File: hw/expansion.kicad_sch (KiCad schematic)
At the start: 2 parts

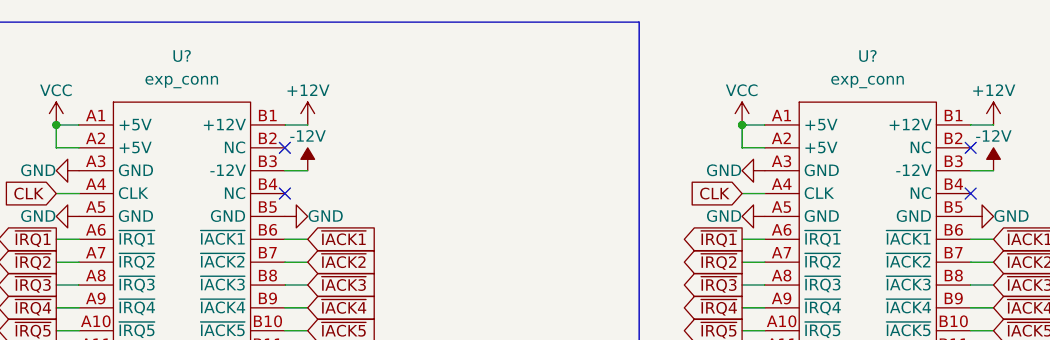
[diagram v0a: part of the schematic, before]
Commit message: fixed ERC errors
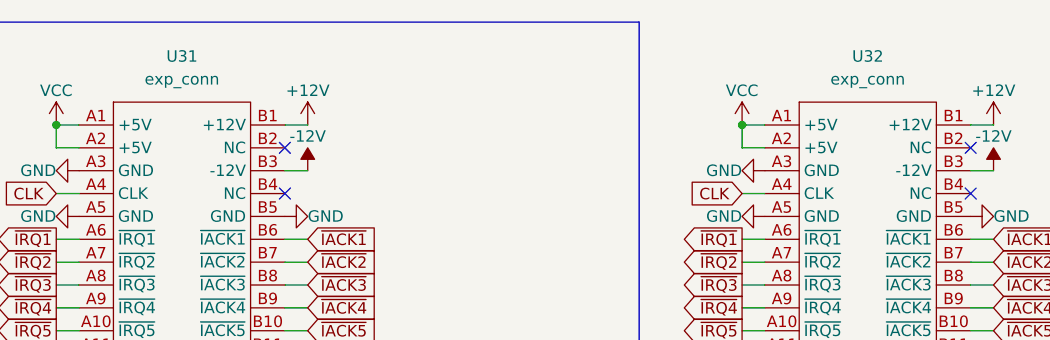
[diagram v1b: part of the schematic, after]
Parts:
- gave numbers to parts that had none: 2
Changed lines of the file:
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@@
   (symbol (lib_id "power:-12V") (at 124.46 33.02 0) (unit 1)
     (in_bom yes) (on_board yes)
-    (property "Reference" "#PWR?" (id 0) (at 124.46 30.48 0)
+    (property "Reference" "#PWR086" (id 0) (at 124.46 30.48 0)
       (effects (font (size 1.27 1.27)) hide)
     )
@@
   (symbol (lib_id "power:GND") (at 121.92 38.1 90) (unit 1)
     (in_bom yes) (on_board yes)
-    (property "Reference" "#PWR?" (id 0) (at 128.27 38.1 0)
+    (property "Reference" "#PWR084" (id 0) (at 128.27 38.1 0)
       (effects (font (size 1.27 1.27)) hide)
     )
@@
   (symbol (lib_id "power:VCC") (at 96.52 27.94 0) (unit 1)
     (in_bom yes) (on_board yes)
-    (property "Reference" "#PWR?" (id 0) (at 96.52 31.75 0)
+    (property "Reference" "#PWR081" (id 0) (at 96.52 31.75 0)
       (effects (font (size 1.27 1.27)) hide)
     )
@@
   (symbol (lib_id "m68kcomp2:exp_conn") (at 110.49 24.13 0) (unit 1)
     (in_bom yes) (on_board yes) (fields_autoplaced)
-    (property "Reference" "U?" (id 0) (at 110.49 20.32 0))
+    (property "Reference" "U31" (id 0) (at 110.49 20.32 0))
     (property "Value" "exp_conn" (id 1) (at 110.49 22.86 0))
     (property "Footprint" "" (id 2) (at 110.49 24.13 0)
@@
   (symbol (lib_id "power:VCC") (at 172.72 27.94 0) (unit 1)
     (in_bom yes) (on_board yes)
-    (property "Reference" "#PWR?" (id 0) (at 172.72 31.75 0)
+    (property "Reference" "#PWR087" (id 0) (at 172.72 31.75 0)
       (effects (font (size 1.27 1.27)) hide)
     )
@@
   (symbol (lib_id "power:+12V") (at 124.46 27.94 0) (unit 1)
     (in_bom yes) (on_board yes)
-    (property "Reference" "#PWR?" (id 0) (at 124.46 31.75 0)
+    (property "Reference" "#PWR085" (id 0) (at 124.46 31.75 0)
       (effects (font (size 1.27 1.27)) hide)
     )
@@
   (symbol (lib_id "power:GND") (at 99.06 38.1 270) (unit 1)
     (in_bom yes) (on_board yes)
-    (property "Reference" "#PWR?" (id 0) (at 92.71 38.1 0)
+    (property "Reference" "#PWR083" (id 0) (at 92.71 38.1 0)
       (effects (font (size 1.27 1.27)) hide)
     )
@@
   (symbol (lib_id "power:GND") (at 198.12 38.1 90) (unit 1)
     (in_bom yes) (on_board yes)
-    (property "Reference" "#PWR?" (id 0) (at 204.47 38.1 0)
+    (property "Reference" "#PWR090" (id 0) (at 204.47 38.1 0)
       (effects (font (size 1.27 1.27)) hide)
     )
@@
   (symbol (lib_id "power:GND") (at 99.06 33.02 270) (unit 1)
     (in_bom yes) (on_board yes)
-    (property "Reference" "#PWR?" (id 0) (at 92.71 33.02 0)
+    (property "Reference" "#PWR082" (id 0) (at 92.71 33.02 0)
       (effects (font (size 1.27 1.27)) hide)
     )
@@
   (symbol (lib_id "power:-12V") (at 200.66 33.02 0) (unit 1)
     (in_bom yes) (on_board yes)
-    (property "Reference" "#PWR?" (id 0) (at 200.66 30.48 0)
+    (property "Reference" "#PWR092" (id 0) (at 200.66 30.48 0)
       (effects (font (size 1.27 1.27)) hide)
     )
@@
   (symbol (lib_id "m68kcomp2:exp_conn") (at 186.69 24.13 0) (unit 1)
     (in_bom yes) (on_board yes) (fields_autoplaced)
-    (property "Reference" "U?" (id 0) (at 186.69 20.32 0))
+    (property "Reference" "U32" (id 0) (at 186.69 20.32 0))
     (property "Value" "exp_conn" (id 1) (at 186.69 22.86 0))
     (property "Footprint" "" (id 2) (at 186.69 24.13 0)
@@
   (symbol (lib_id "power:GND") (at 175.26 38.1 270) (unit 1)
     (in_bom yes) (on_board yes)
-    (property "Reference" "#PWR?" (id 0) (at 168.91 38.1 0)
+    (property "Reference" "#PWR089" (id 0) (at 168.91 38.1 0)
       (effects (font (size 1.27 1.27)) hide)
     )
@@
   (symbol (lib_id "power:GND") (at 175.26 33.02 270) (unit 1)
     (in_bom yes) (on_board yes)
-    (property "Reference" "#PWR?" (id 0) (at 168.91 33.02 0)
+    (property "Reference" "#PWR088" (id 0) (at 168.91 33.02 0)
       (effects (font (size 1.27 1.27)) hide)
     )
@@
   (symbol (lib_id "power:+12V") (at 200.66 27.94 0) (unit 1)
     (in_bom yes) (on_board yes)
-    (property "Reference" "#PWR?" (id 0) (at 200.66 31.75 0)
-      (effects (font (size 1.27 1.27)) hide)
-    )
+    (property "Reference" "#PWR091" (id 0) (at 200.66 31.75 0)
+      (effects (font (size 1.27 1.27)) hide)
+    )

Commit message: added expansion slot footprint (PCI-e 8x)
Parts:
- U31, U32: footprint (none) -> m68kcomp2:pcix8slot
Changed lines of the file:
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@@
     (property "Reference" "U31" (id 0) (at 110.49 20.32 0))
     (property "Value" "exp_conn" (id 1) (at 110.49 22.86 0))
-    (property "Footprint" "" (id 2) (at 110.49 24.13 0)
+    (property "Footprint" "m68kcomp2:pcix8slot" (id 2) (at 110.49 24.13 0)
       (effects (font (size 1.27 1.27)) hide)
     )
@@
     (property "Reference" "U32" (id 0) (at 186.69 20.32 0))
     (property "Value" "exp_conn" (id 1) (at 186.69 22.86 0))
-    (property "Footprint" "" (id 2) (at 186.69 24.13 0)
-      (effects (font (size 1.27 1.27)) hide)
-    )
+    (property "Footprint" "m68kcomp2:pcix8slot" (id 2) (at 186.69 24.13 0)
+      (effects (font (size 1.27 1.27)) hide)
+    )

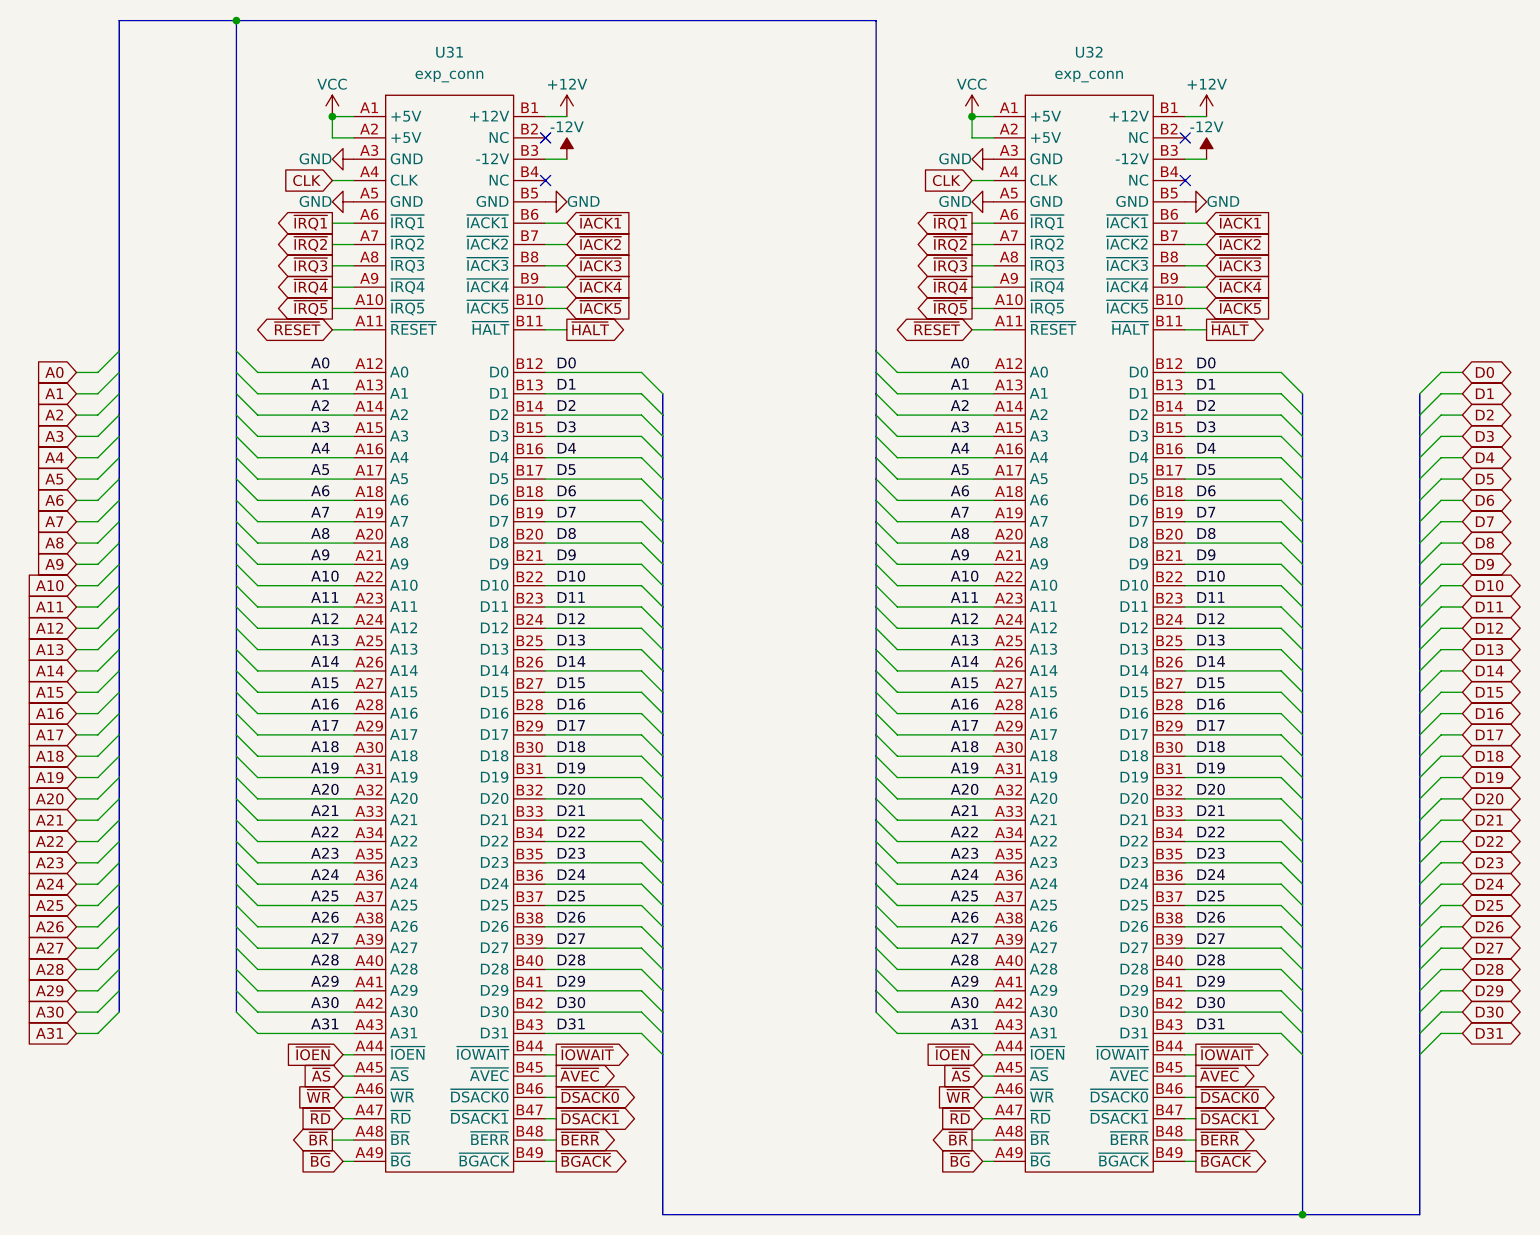
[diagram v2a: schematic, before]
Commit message: 32bit buses take a lot of space
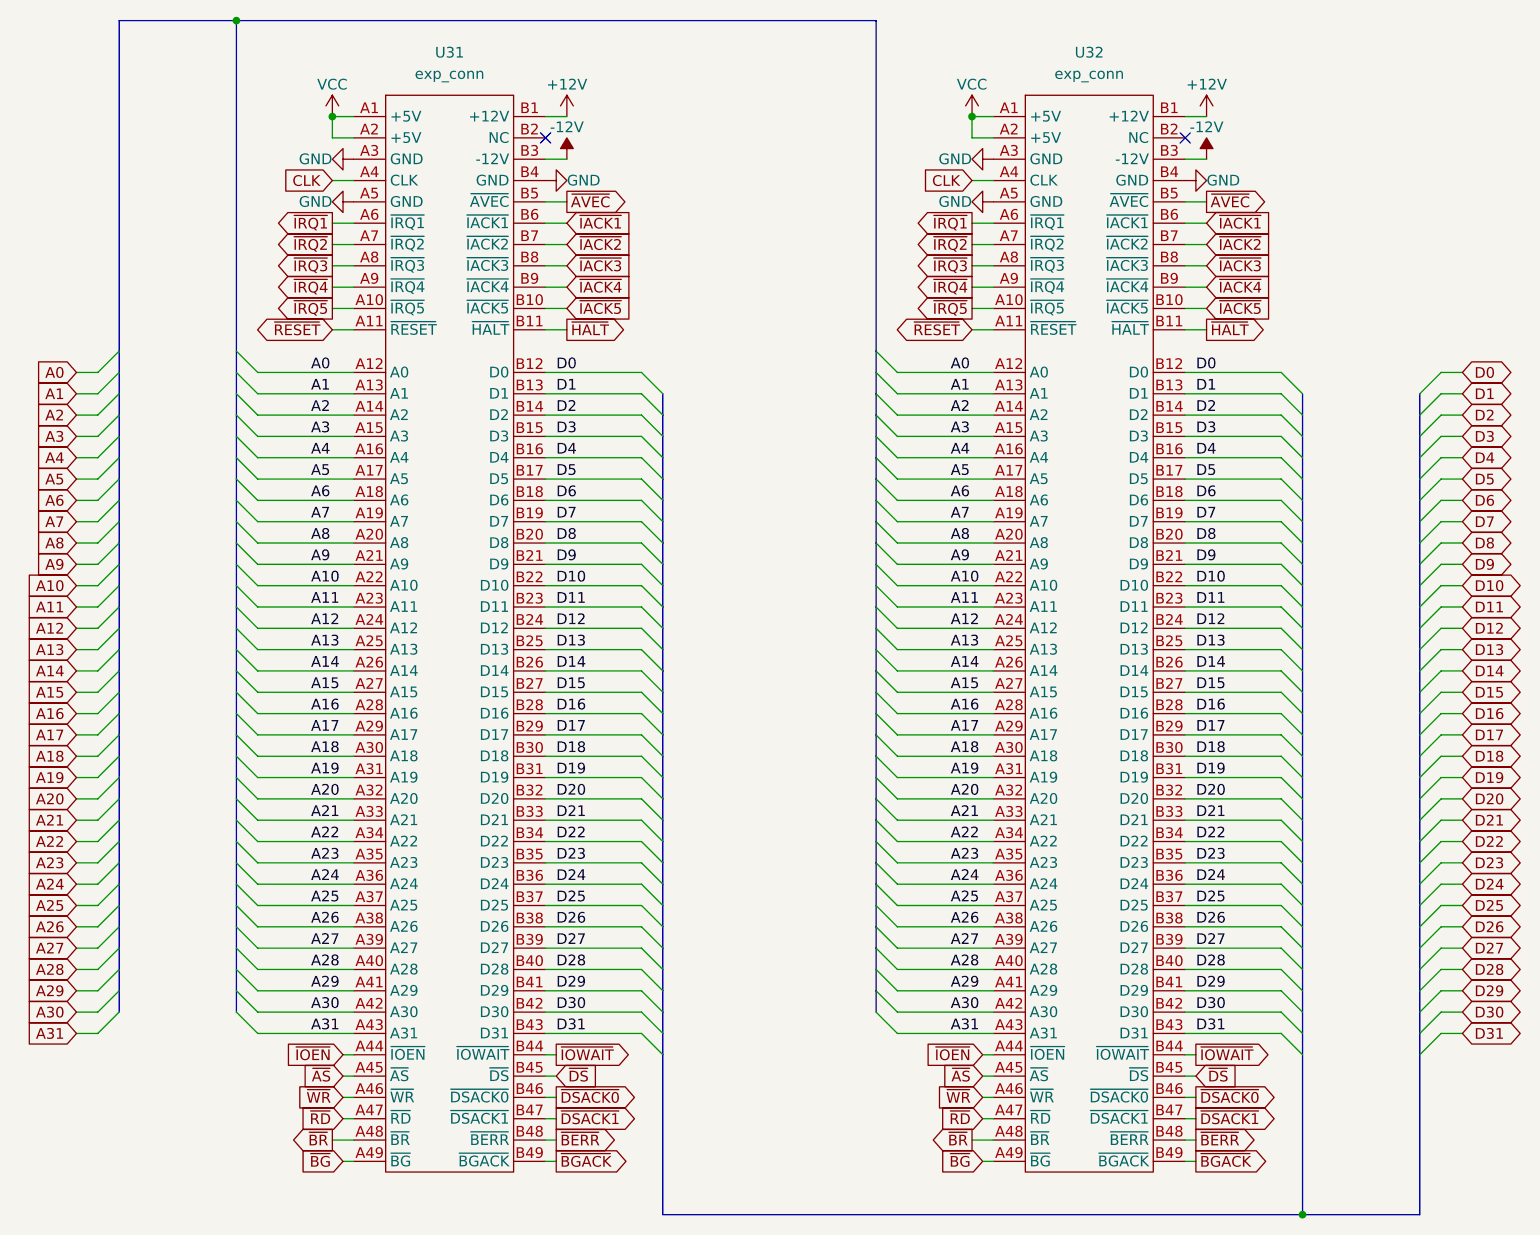
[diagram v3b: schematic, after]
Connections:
- net GND: now also U31.B4 (GND), U32.B4 (GND); no longer U31.B5 (GND), U32.B5 (GND)
- net ~{AVEC}: now also U31.B5 (~{AVEC}), U32.B5 (~{AVEC}); no longer U31.B45 (~{AVEC}), U32.B45 (~{AVEC})
- new net ~{DS}: U31.B45 (~{DS}), U32.B45 (~{DS})
- no-connect marks 4 -> 2
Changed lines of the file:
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@@
   )
   (no_connect (at 121.92 30.48))
-  (no_connect (at 121.92 35.56))
   (no_connect (at 198.12 30.48))
-  (no_connect (at 198.12 35.56))
   (bus_entry (at 226.06 106.68) (size 2.54 -2.54)
     (stroke (width 0) (type default) (color 0 0 0 0))
@@
     (stroke (width 0) (type default) (color 0 0 0 0))
   )
+  (wire (pts (xy 198.12 38.1) (xy 200.66 38.1))
+    (stroke (width 0) (type default) (color 0 0 0 0))
+  )
   (bus (pts (xy 135.89 132.08) (xy 135.89 134.62))
     (stroke (width 0) (type default) (color 0 0 0 0))
@@
     (stroke (width 0) (type default) (color 0 0 0 0))
   )
+  (wire (pts (xy 124.46 38.1) (xy 121.92 38.1))
+    (stroke (width 0) (type default) (color 0 0 0 0))
+  )
   (wire (pts (xy 198.12 78.74) (xy 209.55 78.74))
     (stroke (width 0) (type default) (color 0 0 0 0))
@@
     )
   )
+  (global_label "~{DS}" (shape input) (at 123.19 142.24 0) (fields_autoplaced)
+    (effects (font (size 1.27 1.27)) (justify left))
+    (property "Intersheet References" "${INTERSHEET_REFS}" (id 0) (at 128.0826 142.1606 0)
+      (effects (font (size 1.27 1.27)) (justify left) hide)
+    )
+  )
   (global_label "~{IRQ3}" (shape output) (at 172.72 45.72 180) (fields_autoplaced)
     (effects (font (size 1.27 1.27)) (justify right))
@@
     )
   )
+  (global_label "~{DS}" (shape input) (at 199.39 142.24 0) (fields_autoplaced)
+    (effects (font (size 1.27 1.27)) (justify left))
+    (property "Intersheet References" "${INTERSHEET_REFS}" (id 0) (at 204.2826 142.1606 0)
+      (effects (font (size 1.27 1.27)) (justify left) hide)
+    )
+  )
   (global_label "D0" (shape bidirectional) (at 231.14 58.42 0) (fields_autoplaced)
     (effects (font (size 1.27 1.27)) (justify left))
@@
     )
   )
-  (global_label "~{AVEC}" (shape output) (at 199.39 142.24 0) (fields_autoplaced)
-    (effects (font (size 1.27 1.27)) (justify left))
-    (property "Intersheet References" "${INTERSHEET_REFS}" (id 0) (at 206.3993 142.1606 0)
-      (effects (font (size 1.27 1.27)) (justify left) hide)
-    )
-  )
   (global_label "A31" (shape input) (at 66.04 137.16 180) (fields_autoplaced)
     (effects (font (size 1.27 1.27)) (justify right))
@@
     )
   )
+  (global_label "~{AVEC}" (shape output) (at 200.66 38.1 0) (fields_autoplaced)
+    (effects (font (size 1.27 1.27)) (justify left))
+    (property "Intersheet References" "${INTERSHEET_REFS}" (id 0) (at 207.6693 38.0206 0)
+      (effects (font (size 1.27 1.27)) (justify left) hide)
+    )
+  )
   (global_label "D13" (shape bidirectional) (at 231.14 91.44 0) (fields_autoplaced)
     (effects (font (size 1.27 1.27)) (justify left))
@@
     )
   )
-  (global_label "~{AVEC}" (shape output) (at 123.19 142.24 0) (fields_autoplaced)
+  (global_label "~{AVEC}" (shape output) (at 124.46 38.1 0) (fields_autoplaced)
     (effects (font (size 1.27 1.27)) (justify left))
-    (property "Intersheet References" "${INTERSHEET_REFS}" (id 0) (at 130.1993 142.1606 0)
+    (property "Intersheet References" "${INTERSHEET_REFS}" (id 0) (at 131.4693 38.0206 0)
       (effects (font (size 1.27 1.27)) (justify left) hide)
     )
@@
     (pin "1")
   )
-  (symbol (lib_id "power:GND") (at 121.92 38.1 90) (unit 1)
+  (symbol (lib_id "power:GND") (at 121.92 35.56 90) (unit 1)
     (in_bom yes) (on_board yes)
-    (property "Reference" "#PWR084" (id 0) (at 128.27 38.1 0)
+    (property "Reference" "#PWR084" (id 0) (at 128.27 35.56 0)
       (effects (font (size 1.27 1.27)) hide)
     )
-    (property "Value" "GND" (id 1) (at 124.46 38.1 90)
+    (property "Value" "GND" (id 1) (at 124.46 35.56 90)
       (effects (font (size 1.27 1.27)) (justify right))
     )
-    (property "Footprint" "" (id 2) (at 121.92 38.1 0)
+    (property "Footprint" "" (id 2) (at 121.92 35.56 0)
       (effects (font (size 1.27 1.27)) hide)
     )
-    (property "Datasheet" "" (id 3) (at 121.92 38.1 0)
+    (property "Datasheet" "" (id 3) (at 121.92 35.56 0)
       (effects (font (size 1.27 1.27)) hide)
     )
@@
     (pin "1")
   )
-  (symbol (lib_id "m68kcomp2:exp_conn") (at 110.49 24.13 0) (unit 1)
+  (symbol (lib_name "exp_conn_1") (lib_id "m68kcomp2:exp_conn") (at 110.49 24.13 0) (unit 1)
     (in_bom yes) (on_board yes) (fields_autoplaced)
     (property "Reference" "U31" (id 0) (at 110.49 20.32 0))
@@
     (pin "1")
   )
-  (symbol (lib_id "power:GND") (at 198.12 38.1 90) (unit 1)
+  (symbol (lib_id "power:GND") (at 198.12 35.56 90) (unit 1)
     (in_bom yes) (on_board yes)
-    (property "Reference" "#PWR090" (id 0) (at 204.47 38.1 0)
+    (property "Reference" "#PWR090" (id 0) (at 204.47 35.56 0)
       (effects (font (size 1.27 1.27)) hide)
     )
-    (property "Value" "GND" (id 1) (at 200.66 38.1 90)
+    (property "Value" "GND" (id 1) (at 200.66 35.56 90)
       (effects (font (size 1.27 1.27)) (justify right))
     )
-    (property "Footprint" "" (id 2) (at 198.12 38.1 0)
+    (property "Footprint" "" (id 2) (at 198.12 35.56 0)
       (effects (font (size 1.27 1.27)) hide)
     )
-    (property "Datasheet" "" (id 3) (at 198.12 38.1 0)
+    (property "Datasheet" "" (id 3) (at 198.12 35.56 0)
       (effects (font (size 1.27 1.27)) hide)
     )
